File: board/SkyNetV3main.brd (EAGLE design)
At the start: 160 x 100 mm, 67 parts, among them IC1 HC_05, IC2 RF4463PRO, IC3 LPC1768, IC4 BCX17, IC5 TPS63001, IC6 MCP73871-2CCI/ML, Q1 32.768KHz, Q2 12MHz, Q3 IRLM6402, Q4 BSS138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

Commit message: further layout, got stuck somewhere...
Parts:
- moved U$1 11.1 mm to (42.7, 14.6), turned to 180 degrees
- moved S3 8.02 mm to (32.0, 14.6)
- moved C1 6.14 mm to (44.2, 30.9), flipped to the top, turned to 270 degrees
- moved R10 3.10 mm to (13.5, 51.5)
- moved R9 2.98 mm to (13.5, 49.5)
- moved R1 2.04 mm to (37.2, 60.9), turned to 180 degrees
- moved C18 1.83 mm to (31.2, 46.1)
- moved C17 1.38 mm to (24.2, 46.8)
- moved C21 1.10 mm to (23.2, 52.3)
- moved C12 1.06 mm to (28.0, 52.3)
- moved C13 1.03 mm to (30.5, 52.3)
- moved C14 1.03 mm to (25.4, 52.3)
- moved C20 1.01 mm to (31.2, 44.1), turned to 0 degrees
- moved R8 1.01 mm to (9.48, 46.2)
- moved R7 0.96 mm to (7.36, 46.1)
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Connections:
- removed net BT_RESET: IC1.11, IC3.80
- new net BT-RST: IC1.11, IC3.56
- net AD-PWR: now also IC3.45; no longer IC3.56
- net BT_AT: now also IC3.68; no longer IC3.81
- net CHGSEL_H: now also IC3.27; no longer IC3.95
- net CHGSEL_L: now also IC3.26; no longer IC3.94
- net CHG_S1: now also IC3.48; no longer IC3.93
- net CHG_S2: now also IC3.49; no longer IC3.92
- net SCL_EXT: now also IC3.24; no longer IC3.49
- net SDA_EXT: now also IC3.25; no longer IC3.48
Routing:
- net BT_AT: track 0.00 -> 48.1 mm, vias 0 -> 1
- net INPUT: track 0.00 -> 43.3 mm
- net +3V3: track 32.0 -> 66.4 mm, vias 2 -> 9
- net CHGSEL_H: track 0.00 -> 27.8 mm, vias 0 -> 2
- net USB-CON: track 0.00 -> 25.5 mm, vias 0 -> 3
- net CHGSEL_L: track 0.00 -> 25.3 mm, vias 0 -> 2
- net EXT_PWR: track 0.00 -> 24.6 mm, vias 0 -> 3
- net VCC: track 0.00 -> 24.4 mm
- net RESET: track 44.0 -> 64.8 mm, vias 0 -> 2
- net V+: track 4.85 -> 25.3 mm, vias 0 -> 1
- net JTAG_TDI: track 0.00 -> 19.6 mm, vias 0 -> 2
- net CHG_S2: track 0.00 -> 19.5 mm, vias 0 -> 1
- net +5V: track 12.9 -> 31.6 mm, vias 0 -> 1
- net JTAG_TDO: track 0.00 -> 18.2 mm, vias 0 -> 2
- net BT_TX: track 0.00 -> 17.6 mm, vias 0 -> 1
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
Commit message: board further
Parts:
- moved IC4 22.1 mm to (27.6, 46.1), turned to 0 degrees
- moved R3 20.8 mm to (28.9, 43.1), turned to 180 degrees
- moved R19 20.0 mm to (3.15, 13.8), turned to 180 degrees
- moved R18 18.6 mm to (3.15, 16.4), turned to 180 degrees
- moved R17 18.6 mm to (3.15, 18.9), turned to 180 degrees
- moved X1 16.2 mm to (2.06, 49.8)
- moved R11 15.2 mm to (12.5, 57.2), turned to 90 degrees
- moved JP1 15.1 mm to (16.3, 60.9), turned to 90 degrees
- moved R4 14.1 mm to (23.8, 47.8), turned to 180 degrees
- moved R9 13.1 mm to (2.11, 55.9), flipped to the bottom
- moved C10 12.3 mm to (16.1, 57.4), turned to 180 degrees
- moved R10 11.7 mm to (2.05, 53.9), flipped to the bottom
- moved C9 8.61 mm to (2.26, 55.0), turned to 90 degrees
- moved C7 8.23 mm to (10.1, 60.3), turned to 180 degrees
- moved C6 5.13 mm to (4.74, 45.3), turned to 180 degrees
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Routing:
- net +3V3: track 66.4 -> 193.3 mm, vias 9 -> 16
- net LED_B: track 0.00 -> 50.0 mm, vias 0 -> 2
- net LED_G: track 0.00 -> 42.1 mm, vias 0 -> 2
- net LED_R: track 0.00 -> 38.9 mm, vias 0 -> 2
- net SCL_EXT: track 0.00 -> 35.0 mm, vias 0 -> 2
- net SDA_EXT: track 0.00 -> 30.5 mm, vias 0 -> 2
- net EXT_GPIO0: track 0.00 -> 24.1 mm, vias 0 -> 2
- net USB-CON: track 25.5 -> 2.73 mm, vias 3 -> 1
- net EXT_GPIO1: track 0.00 -> 22.0 mm, vias 0 -> 2
- net USB-D+: track 4.19 -> 24.6 mm, vias 0 -> 1
- net RF-GPIO0: track 0.00 -> 18.4 mm, vias 0 -> 2
- net CHGSEL_H: track 27.8 -> 9.55 mm
- net CHGSEL_L: track 25.3 -> 9.77 mm
- net +5V: track 31.6 -> 44.3 mm, vias 1 -> 4
- net VCC: track 24.4 -> 11.8 mm
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
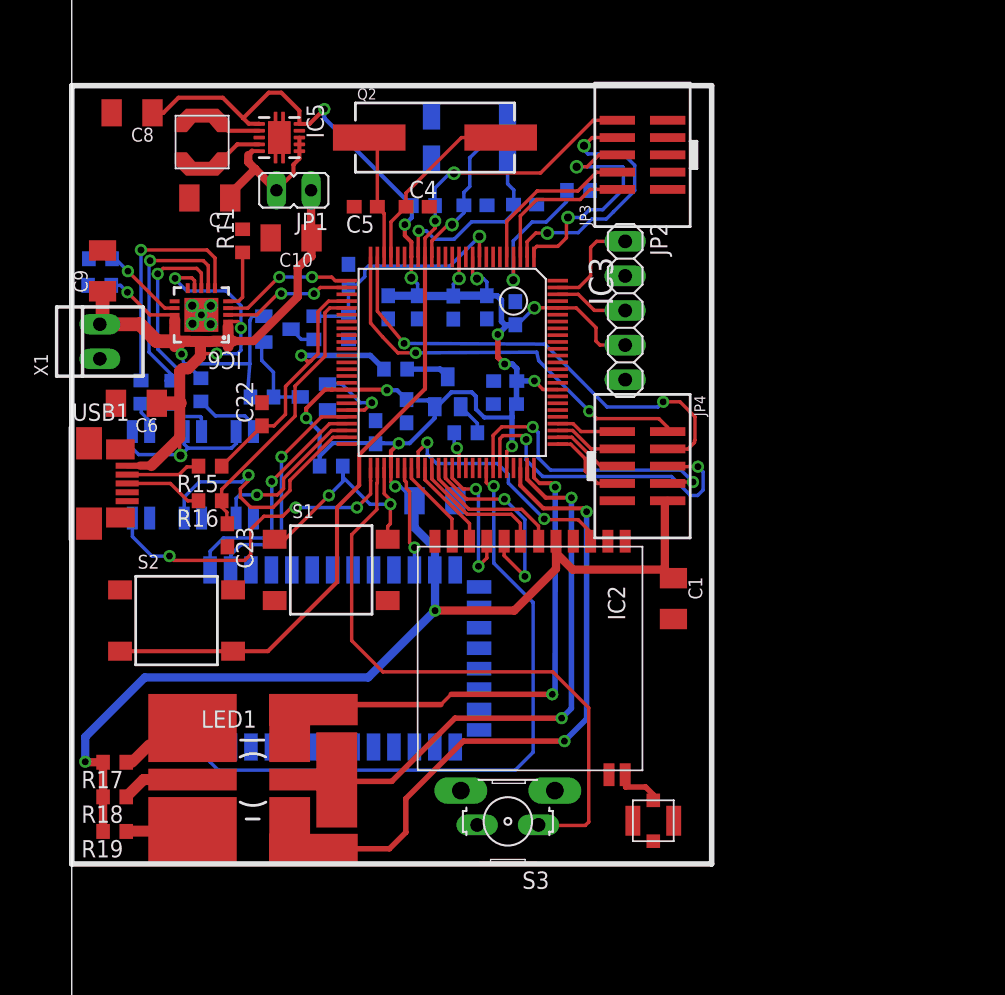
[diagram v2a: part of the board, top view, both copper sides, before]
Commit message: added ground planes
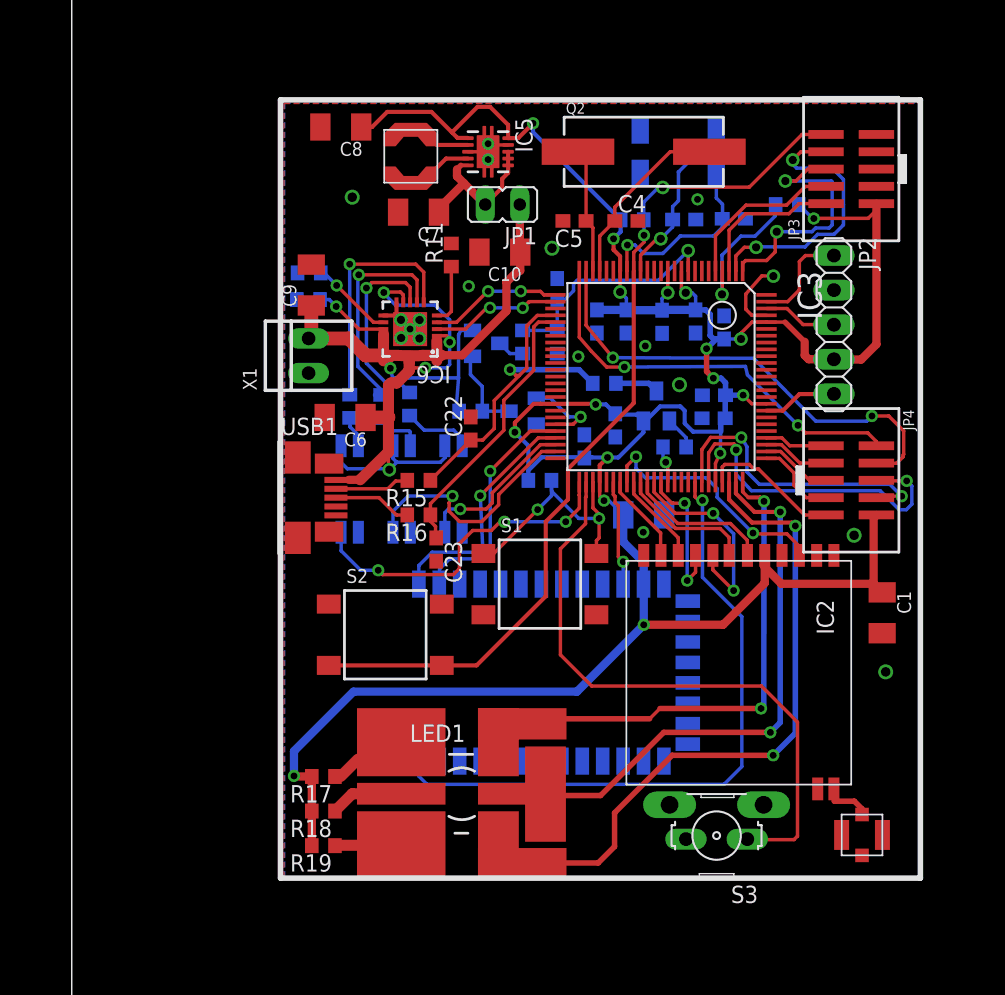
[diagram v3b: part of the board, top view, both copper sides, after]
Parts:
- moved C12 15.4 mm to (43.3, 51.2)
- moved C14 15.4 mm to (40.7, 51.3)
- moved C17 15.4 mm to (39.9, 43.6)
- moved C3 15.4 mm to (48.6, 58.8)
- moved C4 15.4 mm to (40.7, 58.6)
- moved JP3 15.4 mm to (57.2, 62.5)
- moved JP4 15.4 mm to (57.2, 39.6)
- moved R2 15.4 mm to (41.2, 58.7)
- moved S3 15.4 mm to (47.4, 13.5)
- moved C13 15.4 mm to (45.8, 51.3)
- moved C19 15.4 mm to (37.6, 42.1)
- moved C21 15.4 mm to (38.6, 51.3)
- moved C23 15.4 mm to (26.8, 34.5)
- moved C5 15.4 mm to (36.9, 58.6)
- moved C8 15.4 mm to (19.8, 65.5)
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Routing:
- net GND: track 0.00 -> 27.3 mm, vias 1 -> 18
- net +3V3: track 193.3 -> 214.2 mm, vias 16 -> 17
- net CHG_S2: track 19.5 -> 18.2 mm
- net JTAG_TDO: track 18.2 -> 19.2 mm
- net JTAG_TDI: track 19.6 -> 20.5 mm
- net EXT_GPIO0: track 24.1 -> 24.9 mm
- added copper zone on layer 1, net GND
- added copper zone on layer 16, net GND

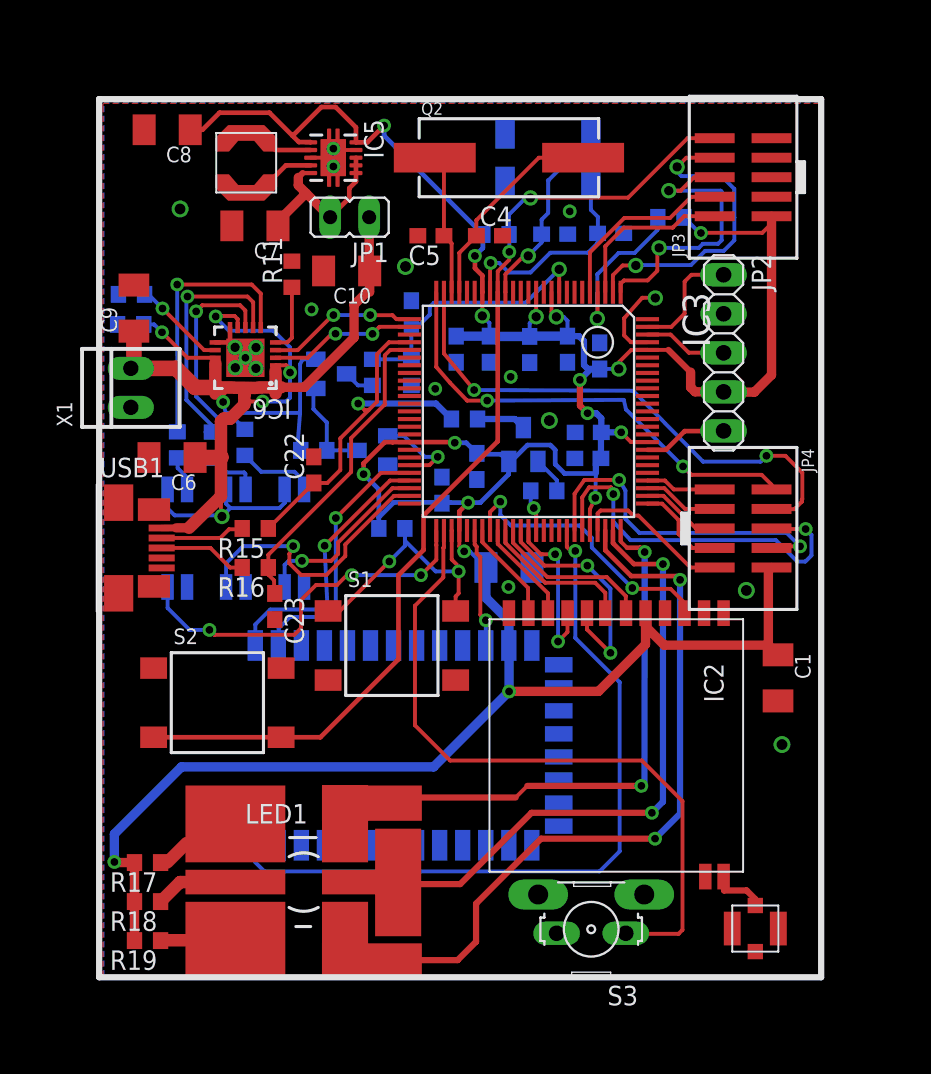
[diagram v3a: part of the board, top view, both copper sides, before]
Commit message: layout optimizations, tStop corrected
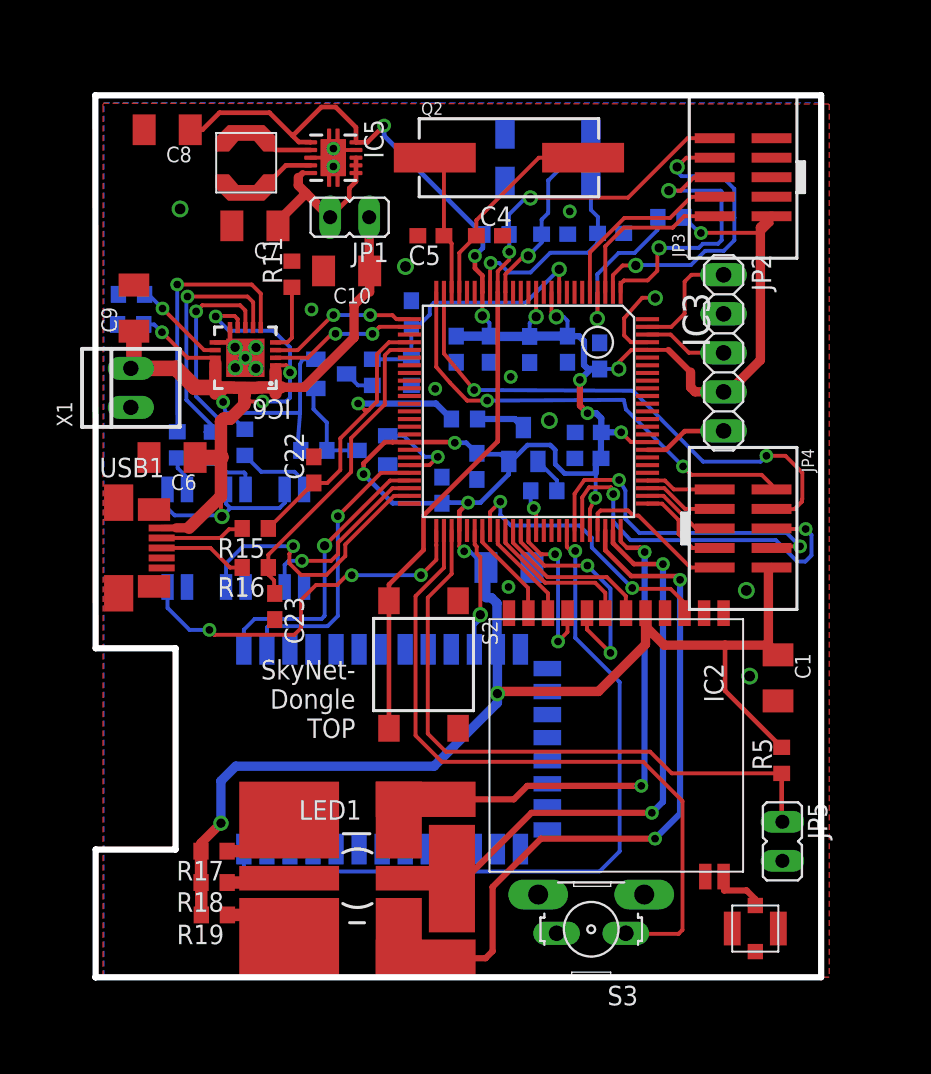
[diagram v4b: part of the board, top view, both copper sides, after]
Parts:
- removed S1: PROG, switch-ck:PTS645-SMD
- added JP5: PROG, jumper:JP1
- moved R5 29.5 mm to (59.7, 24.5), flipped to the top, turned to 90 degrees
- moved S2 13.6 mm to (36.4, 30.7), turned to 270 degrees
- moved R19 4.66 mm to (22.8, 14.4)
- moved R18 4.51 mm to (22.8, 16.6)
- moved R17 4.39 mm to (22.8, 18.6)
- moved LED1 3.51 mm to (32.1, 16.8)
- moved IC1 0.78 mm to (28.6, 25.4)
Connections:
- net GND: now also JP5.2; no longer S1.3, S1.4
- net PROG: now also JP5.1; no longer S1.1, S1.2
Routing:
- net PROG: track 18.5 -> 41.1 mm, vias 2 -> 0
- net RESET: track 65.4 -> 52.1 mm
- net LED_R: track 38.9 -> 34.6 mm
- net +3V3: track 214.2 -> 210.6 mm
- net LED_G: track 42.1 -> 38.7 mm
- net LED_B: track 50.0 -> 47.5 mm
- net BT_RX: track 17.2 -> 18.7 mm
- net LED-G-R: track 5.39 -> 4.15 mm
- net BT_TX: track 17.7 -> 18.7 mm
- net LED-R-R: track 5.63 -> 4.88 mm
- net BT_AT: track 48.1 -> 48.8 mm
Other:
- outline, holes or cut-outs redrawn
- board text added: "SkyNet- Dongle TOP"
- board text added: "SkyNet-Dongle BOTTOM"

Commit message: new layout
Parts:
- removed C14: 100n, rcl:C0603
- removed JP1: MEASURE, jumper:JP1
- removed JP2: DEBUG, pinhead:1X05
- removed JP4: PERIPH, microbuilder:2X05_1.27MM_SMT
- removed JP5: PROG, jumper:JP1
- removed LED1: STATUS, skynet_other:PLCC-6
- removed OK1, OK2, OK3: PC3H7, skynet_other:PC3H7
- removed R7, R8: 91, rcl:R0603
- removed S3: INPUT, skynet_other:PTS645-VERT
- added D1: 3v3, diode:SOT23
- added LED2: RGBLED5050, adafruit:RGBLED5050
- added S1: INPUT, switch-ck:PTS645-SMD
- added SJ1: (no value), jumper:SJ
- added SJ2: PROG, jumper:SJ
- added U$2: (no value), skynet_other:PIN-HEAD-1X3-SMD
- C12, C13: value 100n -> 100u; device rcl:C0603 -> microbuilder:EIA6032-28/C-W
- C4, C5: value 33p -> 18p
- Q1: device crystal-2:MM20SS -> skynet_other:XTAL_49_18
- Q2: device microbuilder:HC49UP -> skynet_other:XTAL_50_32
- R6: value 91 -> 10k
- moved R6 106.8 mm to (123.1, 74.5), flipped to the top, turned to 90 degrees
- moved C8 105.6 mm to (118.9, 29.2), turned to 270 degrees
- moved R18 105.3 mm to (102.1, 85.9), turned to 90 degrees
- moved R19 103.7 mm to (98.0, 85.9), turned to 90 degrees
- moved R17 102.4 mm to (100.1, 85.9), turned to 90 degrees
- moved R16 99.8 mm to (120.5, 67.4), turned to 0 degrees
- moved C23 98.7 mm to (120.5, 65.4), turned to 0 degrees
- moved R15 97.5 mm to (120.5, 61.3), turned to 0 degrees
- moved C7 95.0 mm to (115.6, 29.2), turned to 270 degrees
- moved C22 93.4 mm to (120.5, 63.3), turned to 0 degrees
- moved USB1 92.5 mm to (107.9, 23.5), turned to 90 degrees
- moved L1 85.4 mm to (105.4, 38.6)
- moved IC5 85.3 mm to (111.6, 37.2), turned to 180 degrees
- moved R4 82.4 mm to (120.5, 59.3), flipped to the top, turned to 0 degrees
- moved C6 81.3 mm to (100.4, 31.4), turned to 0 degrees
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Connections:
- net BT_AT renamed BT-AT
- net BT_RX renamed BT-RX
- net BT_TX renamed BT-TX
- net RTCX2 renamed N$2
- net SDI renamed RF-SDI
- net SPI0-NIRQ renamed RF-NIRQ
- net SPI0-NSEL renamed RF-NSEL
- net SPI0-SCLK renamed RF-SCLK
- net SPI0-SDN renamed RF-SDN
- net SPI0-SDO renamed RF-SDO
- removed net BT-RST: IC1.11, IC3.56
- removed net CHGSEL_H: IC3.27, IC6.3
- removed net CHGSEL_L: IC3.26, IC6.4
- removed net CHG_S1: IC3.48, OK3.4
- removed net CHG_S2: IC3.49, OK2.4
- removed net EXT_GPIO0: IC3.70, JP4.6
- removed net EXT_GPIO1: IC3.69, JP4.8
- removed net EXT_PWR: IC3.51, OK1.4
- removed net LED_B: IC3.73, LED1.6, LED1.6@1
- removed net LED_G: IC3.74, LED1.5, LED1.5@1
- removed net LED_R: IC3.75, LED1.4, LED1.4@1
- removed net PG: IC6.6, R6.1
- removed net PG-OK: OK1.2, R6.2
- removed net SCL_EXT: IC3.24, JP4.4
- removed net SDA_EXT: IC3.25, JP4.2
- removed net SPI2_MISO: IC3.77, JP4.5
- removed net SPI2_MOSI: IC3.76, JP4.7
- removed net SPI2_SCK: IC3.78, JP4.3
- removed net SPI2_SEL: IC3.79, JP4.1
- removed net STAT1: IC6.8, R8.1
- removed net STAT1-OK: OK3.2, R8.2
- removed net STAT2: IC6.7, R7.1
- removed net STAT2-OK: OK2.2, R7.2
- new net BT-RESET: IC1.11, IC3.95
- new net CHG-S1: IC3.48, IC6.8
- new net CHG-S2: IC3.49, IC6.7
- new net CHGSEL-H: IC3.7, IC6.3
- new net CHGSEL-L: IC3.6, IC6.4
- new net EXT-PWR: D1.3, IC3.51, R6.2
- new net LED-B: IC3.75, LED2.4
- new net LED-G: IC3.73, LED2.6
- new net LED-R: IC3.74, LED2.5
- new net SCL-EXT: IC3.24, U$2.4
- new net SDA-EXT: IC3.25, U$2.3
- net +3V3: now also C12.+, C13.+, U$2.5; no longer C12.1, C13.1, C14.1, JP2.4, JP4.10
- net +5V: now also R6.1; no longer OK1.1, OK2.1, OK3.1
- net GND: now also C12.-, C13.-, D1.1, S1.3, S1.4, SJ2.1, U$2.6; no longer C12.2, C13.2, C14.2, JP2.5, JP4.9, JP5.2, OK1.3, OK2.3, OK3.3, S3.2
- net INPUT: now also S1.1, S1.2; no longer S3.1
- net LED-B-R: now also LED2.3; no longer LED1.3
- net LED-G-R: now also LED2.1; no longer LED1.2
- net LED-R-R: now also LED2.2; no longer LED1.1
- net OUT2: now also SJ1.1; no longer JP1.1
- net PROG: now also SJ2.2; no longer JP5.1
- net RTCX1: now also Q1.2; no longer Q1.4
- net RX: now also U$2.1; no longer JP2.1
- net TX: now also U$2.2; no longer JP2.3
- net VCC: now also SJ1.2; no longer JP1.2
- net XTAL1: now also Q2.3; no longer Q2.2
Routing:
- net CHG-S2: track 0.00 -> 88.7 mm, vias 0 -> 4
- net CHG-S1: track 0.00 -> 87.3 mm, vias 0 -> 4
- net +5V: track 44.3 -> 120.7 mm, vias 4 -> 5
- net BT-RX: track 18.7 -> 90.8 mm, vias 1 -> 3
- net BT-TX: track 18.7 -> 84.7 mm, vias 1 -> 3
- net USB-D-_IN: track 5.77 -> 71.2 mm
- net USB-D+_IN: track 5.50 -> 64.2 mm
- net RF-SDN: track 6.82 -> 55.4 mm, vias 0 -> 1
- net LED_B: track 47.5 -> 0.00 mm, vias 2 -> 0
- net RF-NIRQ: track 6.98 -> 54.1 mm, vias 0 -> 1
- net RF-NSEL: track 10.7 -> 53.9 mm, vias 2 -> 1
- net LED_G: track 38.7 -> 0.00 mm, vias 2 -> 0
- net RF-SDI: track 10.2 -> 48.0 mm, vias 0 -> 1
- net CHGSEL-H: track 0.00 -> 35.9 mm, vias 0 -> 2
- net RF-SCLK: track 15.2 -> 51.1 mm, vias 2 -> 1
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- removed copper zone on layer 1, net GND
- removed copper zone on layer 16, net GND
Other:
- outline, holes or cut-outs redrawn
- board text added: "14650"
- board text added: "2x 18650"
- board text removed: "SkyNet- Dongle TOP"
- board text removed: "SkyNet-Dongle BOTTOM"

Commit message: another layout try, looks much better now
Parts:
- removed U$2: (no value), skynet_other:PIN-HEAD-1X3-SMD
- added JP4: (no value), skynet_other:PIN-HEAD-1X3-SMD
- moved C13 118.4 mm to (108.0, 33.6), turned to 90 degrees
- moved R19 53.0 mm to (124.1, 39.8), turned to 270 degrees
- moved R17 51.0 mm to (122.0, 39.8), turned to 270 degrees
- moved R18 49.4 mm to (120.0, 39.8), turned to 270 degrees
- moved LED2 41.8 mm to (122.0, 45.0), turned to 90 degrees
- moved R5 36.9 mm to (109.6, 49.7), turned to 0 degrees
- moved S1 35.8 mm to (112.6, 45.1), turned to 0 degrees
- moved Q2 34.8 mm to (94.9, 81.3), turned to 180 degrees
- moved Q1 34.7 mm to (104.8, 82.2), turned to 180 degrees
- moved SJ2 34.0 mm to (114.2, 50.2), turned to 180 degrees
- moved S2 33.2 mm to (94.9, 78.9), turned to 90 degrees
- moved R6 33.1 mm to (102.4, 48.7)
- moved R2 32.3 mm to (103.9, 77.5), turned to 270 degrees
- moved JP3 31.6 mm to (114.1, 79.4), turned to 180 degrees
- moved D1 30.4 mm to (99.9, 51.0), turned to 270 degrees
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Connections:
- net N$2 renamed RTCX2
- net +3V3: now also JP4.5; no longer U$2.5
- net AD-PWR: now also IC3.95; no longer IC3.45
- net BT-AT: now also IC3.50; no longer IC3.68
- net BT-RESET: now also IC3.49; no longer IC3.95
- net CHG-S1: now also IC3.56; no longer IC3.48
- net CHG-S2: now also IC3.57; no longer IC3.49
- net CHGSEL-H: now also IC3.70; no longer IC3.7
- net CHGSEL-L: now also IC3.69; no longer IC3.6
- net GND: now also JP4.6; no longer U$2.6
- net RF-SDN: now also IC3.65; no longer IC3.57
- net RX: now also JP4.2; no longer U$2.1
- net SCL-EXT: now also JP4.4; no longer U$2.4
- net SDA-EXT: now also JP4.3; no longer U$2.3
- net TX: now also JP4.1; no longer U$2.2
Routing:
- net +5V: track 120.7 -> 45.8 mm, vias 5 -> 4
- net V+: track 35.4 -> 94.6 mm, vias 0 -> 4
- net CHG-S2: track 88.7 -> 32.0 mm, vias 4 -> 2
- net CHG-S1: track 87.3 -> 31.2 mm, vias 4 -> 2
- net BT-RX: track 90.8 -> 40.3 mm, vias 3 -> 1
- net BT-TX: track 84.7 -> 42.5 mm, vias 3 -> 1
- net RF-SDN: track 55.4 -> 24.5 mm
- net RF-NSEL: track 53.9 -> 23.6 mm
- net SDA-EXT: track 0.00 -> 30.0 mm, vias 0 -> 2
- net RF-SCLK: track 51.1 -> 22.8 mm
- net GND: track 0.00 -> 26.9 mm, vias 6 -> 62
- net RF-NIRQ: track 54.1 -> 27.2 mm
- net RF-GPIO0: track 47.4 -> 21.0 mm
- net RF-SDI: track 48.0 -> 23.7 mm
- net RF-SDO: track 40.6 -> 22.0 mm
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- added copper zone on layer 1, net GND
- added copper zone on layer 16, net GND

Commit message: layout improvements
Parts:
- moved L1 5.56 mm to (114.2, 38.7), turned to 0 degrees
- moved JP4 1.42 mm to (123.0, 72.2)
- moved USB1 1.04 mm to (109.2, 19.5)
- moved S1 0.59 mm to (112.0, 45.0)
- moved JP3 0.38 mm to (113.7, 79.4)
- moved U$1 0.15 mm to (116.0, 20.5)
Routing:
- net GND: track 26.9 -> 31.9 mm, vias 62 -> 73
- net SDA-EXT: track 30.0 -> 25.0 mm
- net L2: track 7.72 -> 3.36 mm
- net +5V: track 45.8 -> 49.1 mm
- net L1: track 6.08 -> 3.24 mm
- net N$1: track 0.00 -> 1.65 mm
- net AD-PWR: track 15.6 -> 17.2 mm
- net TX: track 7.90 -> 9.34 mm
- net RX: track 4.01 -> 5.45 mm
- net SCL-EXT: track 18.7 -> 20.2 mm
- net INPUT: track 27.0 -> 28.3 mm
- net USB-D-_IN: track 63.9 -> 65.0 mm
- net USB-D+_IN: track 68.1 -> 69.1 mm
- net CHG-S2: track 32.0 -> 31.0 mm
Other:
- outline, holes or cut-outs redrawn
